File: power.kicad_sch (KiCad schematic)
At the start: 0 parts

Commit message: Adicionando novos datasheets e comecando power
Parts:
- added C32, C33, C34, C36, C38, C39, C40, C42, C43: 10u, symbol Device:C
- added C35, C37, C41: 120p, symbol Device:C
- added L1, L2, L3: 470n, symbol Device:L
- added R26, R27, R28, R29, R30, R31: R, symbol Device:R
- added U10, U11, U12: TPS62823DLC, Package_SON:Texas_VSON-HR-8_1.5x2mm_P0.5mm, symbol Regulator_Switching:TPS62823DLC
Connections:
- new net: C41.2, R30.2, R31.1, U12.2 (FB)
- new net: C35.2, R26.2, R27.1, U10.2 (FB)
- new net: L2.1, U11.6 (SW)
- new net: L1.1, U10.6 (SW)
- new net: C37.2, R28.2, R29.1, U11.2 (FB)
- new net: L3.1, U12.6 (SW)
- new net +1V35: C41.1, C42.1, C43.1, L3.2, R30.1
- new net +1V8: C37.1, C38.1, C39.1, L2.2, R28.1
- new net +3V3: C33.1, C34.1, C35.1, L1.2, R26.1
- new net +5V: C32.1, C36.1, C40.1, U10.1 (EN), U10.7 (VIN), U11.1 (EN), U11.7 (VIN), U12.1 (EN), U12.7 (VIN)
- new net GND: C32.2, C33.2, C34.2, C36.2, C38.2, C39.2, C40.2, C42.2, C43.2, R27.2, R29.2, R31.2, U10.3 (AGND), U10.5 (PGND), U11.3 (AGND), U11.5 (PGND), U12.3 (AGND), U12.5 (PGND)
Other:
- title: ECP5 85F Platonic Board -> PatchLogic 85 FPGA Board

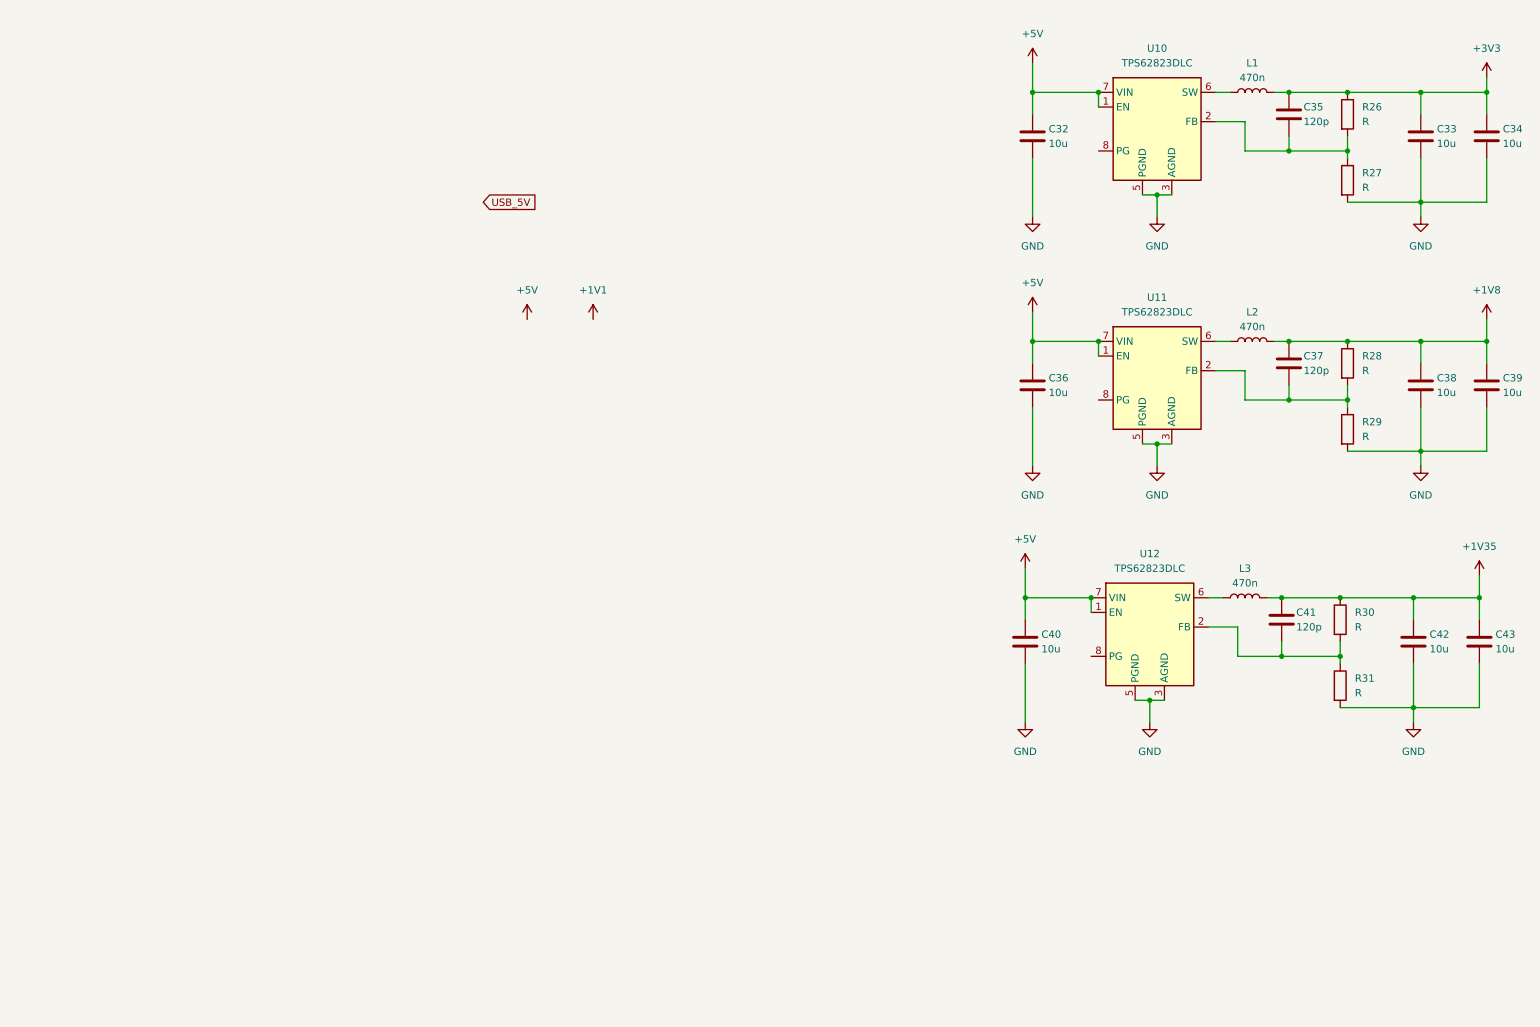
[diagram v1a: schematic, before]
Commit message: Implementando power e ligando jtag e flash a fpga
Implementando circuito de power. Ligando JTAG e memoria FLASH quad SPI a
FPGA. Iniciando implementacão da DRAM e outros modulos
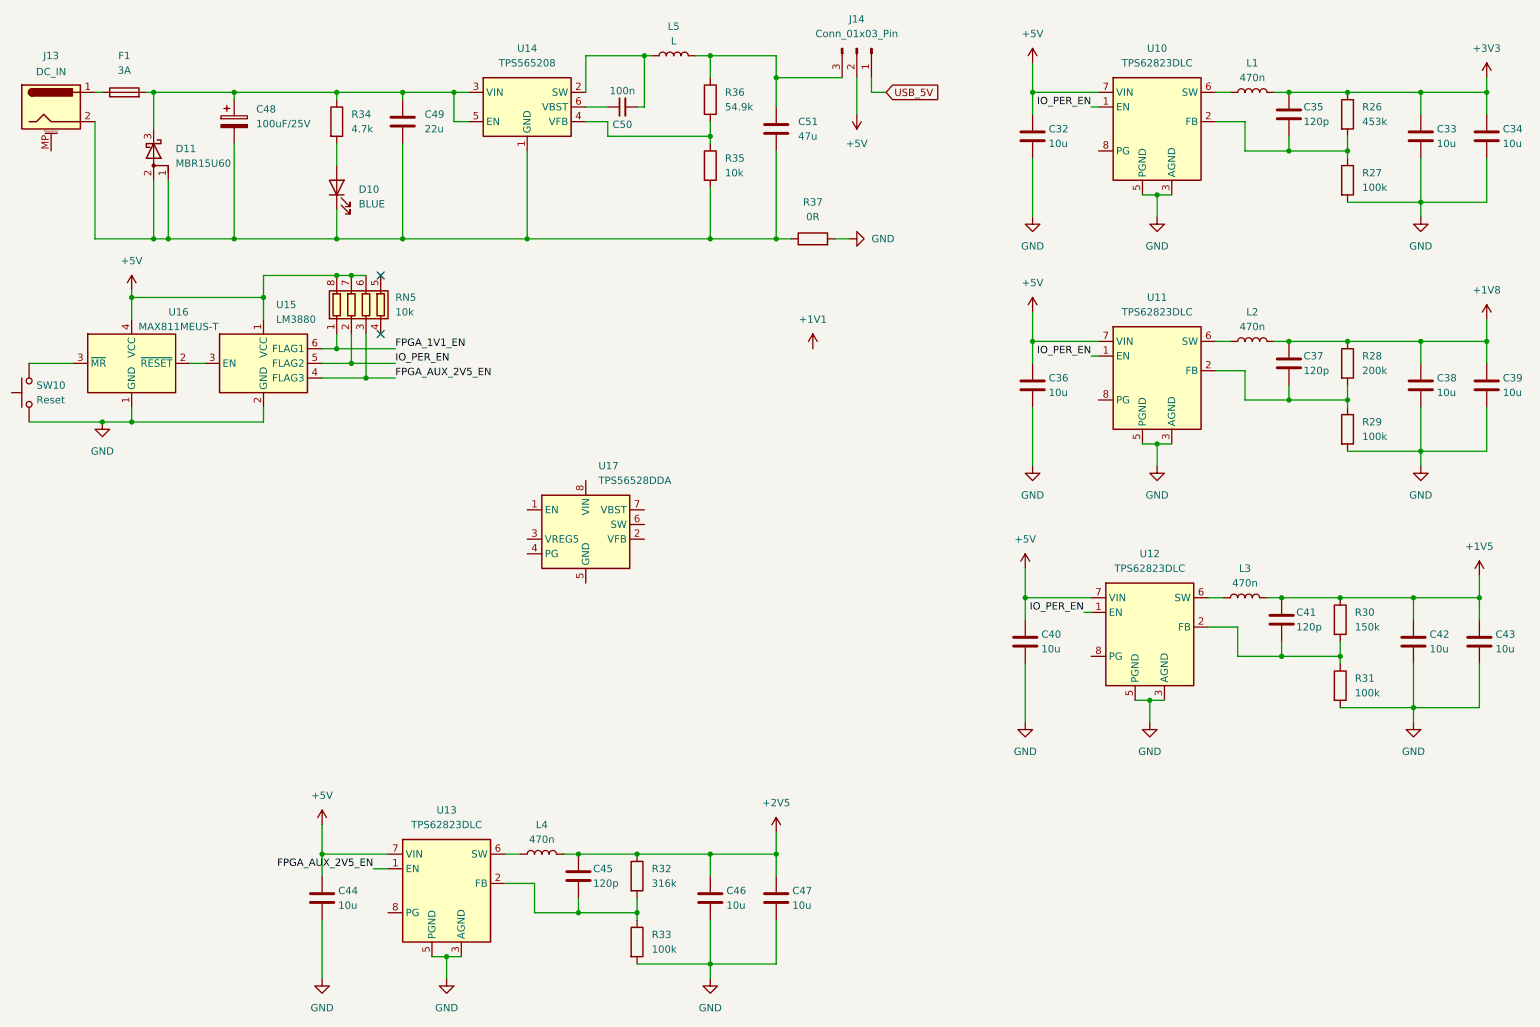
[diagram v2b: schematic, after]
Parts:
- added C44, C46, C47: 10u, symbol Device:C
- added C45: 120p, symbol Device:C
- added C48: 100uF/25V, Capacitor_SMD:CP_Elec_4x4.5, symbol Device:C_Polarized
- added C49: 22u, symbol Device:C
- added C50: 100n, symbol Device:C_Small
- added C51: 47u, symbol Device:C
- added D10: BLUE, symbol Device:LED
- added D11: MBR15U60, Diode_SMD:D_SMB_Modified, symbol Device:D_Schottky_AAK
- added F1: 3A, Fuse:Fuse_1206_3216Metric_Pad1.42x1.75mm_HandSolder, symbol Device:Fuse
- added J13: DC_IN, Connector_BarrelJack:BarrelJack_Horizontal, symbol Connector:Barrel_Jack_MountingPin
- added J14: Conn_01x03_Pin, Connector_PinHeader_2.54mm:PinHeader_1x03_P2.54mm_Vertical, symbol Connector:Conn_01x03_Pin
- added L4: 470n, symbol Device:L
- added L5: L, symbol Device:L
- added R32: 316k, symbol Device:R
- added R33: 100k, symbol Device:R
- added R34: 4.7k, symbol Device:R
- added R35: 10k, symbol Device:R
- added R36: 54.9k, symbol Device:R
- added R37: 0R, symbol Device:R
- added RN5: 10k, Resistor_SMD:R_Array_Convex_4x0402, symbol Device:R_Pack04
- added SW10: Reset, symbol Switch:SW_Push
- added U13: TPS62823DLC, Package_SON:Texas_VSON-HR-8_1.5x2mm_P0.5mm, symbol Regulator_Switching:TPS62823DLC
- added U14: TPS565208, Package_TO_SOT_SMD:SOT-23-6, symbol Regulator_Switching:TPS565208
- added U15: LM3880, Package_TO_SOT_SMD:SOT-23-6, symbol Power_Supervisor:LM3880
- added U16: MAX811MEUS-T, Package_TO_SOT_SMD:SOT-143, symbol Power_Supervisor:MAX811MEUS-T
- added U17: TPS56528DDA, Package_SO:Texas_HSOP-8-1EP_3.9x4.9mm_P1.27mm_ThermalVias, symbol Regulator_Switching:TPS56528DDA
- R26: value R -> 453k
- R27, R29, R31: value R -> 100k
- R28: value R -> 200k
- R30: value R -> 150k
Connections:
- net +5V: now also C44.1, J14.2 (Pin_2), RN5.6 (R3.2), RN5.7 (R2.2), RN5.8 (R1.2), U13.7 (VIN), U15.1 (VCC), U16.4 (VCC); no longer U10.1 (EN), U11.1 (EN), U12.1 (EN)
- net GND: now also C44.2, C46.2, C47.2, R33.2, R37.2, SW10.1, U13.3 (AGND), U13.5 (PGND), U15.2 (GND), U16.1 (GND)
- net USB_5V: now also J14.1 (Pin_1)
- net +1V35 renamed +1V5
- new net: C48.2, C49.2, C51.2, D10.1 (K), D11.1 (A), D11.2 (A), J13.2, R35.2, R37.1, U14.1 (GND)
- new net: C48.1, C49.1, D11.3 (K), F1.2, R34.1, U14.3 (VIN), U14.5 (EN)
- new net: U15.3 (EN), U16.2 (~{RESET})
- new net: SW10.2, U16.3 (~{MR})
- new net: D10.2 (A), R34.2
- new net: C45.2, R32.2, R33.1, U13.2 (FB)
- new net: L4.1, U13.6 (SW)
- new net: C50.2, L5.1, U14.2 (SW)
- new net: R35.1, R36.2, U14.4 (VFB)
- new net: C50.1, U14.6 (VBST)
- new net: U17.5 (GND), U17.9 (GND)
- new net: F1.1, J13.1
- new net: C51.1, J14.3 (Pin_3), L5.2, R36.1
- new net +2V5: C45.1, C46.1, C47.1, L4.2, R32.1
- new net FPGA_1V1_EN: RN5.1 (R1.1), U15.6 (FLAG1)
- new net FPGA_AUX_2V5_EN: RN5.3 (R3.1), U13.1 (EN), U15.4 (FLAG3)
- new net IO_PER_EN: RN5.2 (R2.1), U10.1 (EN), U11.1 (EN), U12.1 (EN), U15.5 (FLAG2)
- no-connect marks 0 -> 2
